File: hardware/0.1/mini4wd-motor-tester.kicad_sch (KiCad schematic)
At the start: 102 parts, among them J1 USB_C_Receptacle_USB2.0_16P, J2 JST SH, J3 JST SH, J4 JST XH, M1 Motor_DC, Q2 AO3401A, Q3 2N7002, SW1 RA, SW2 RA, SW3 EC11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

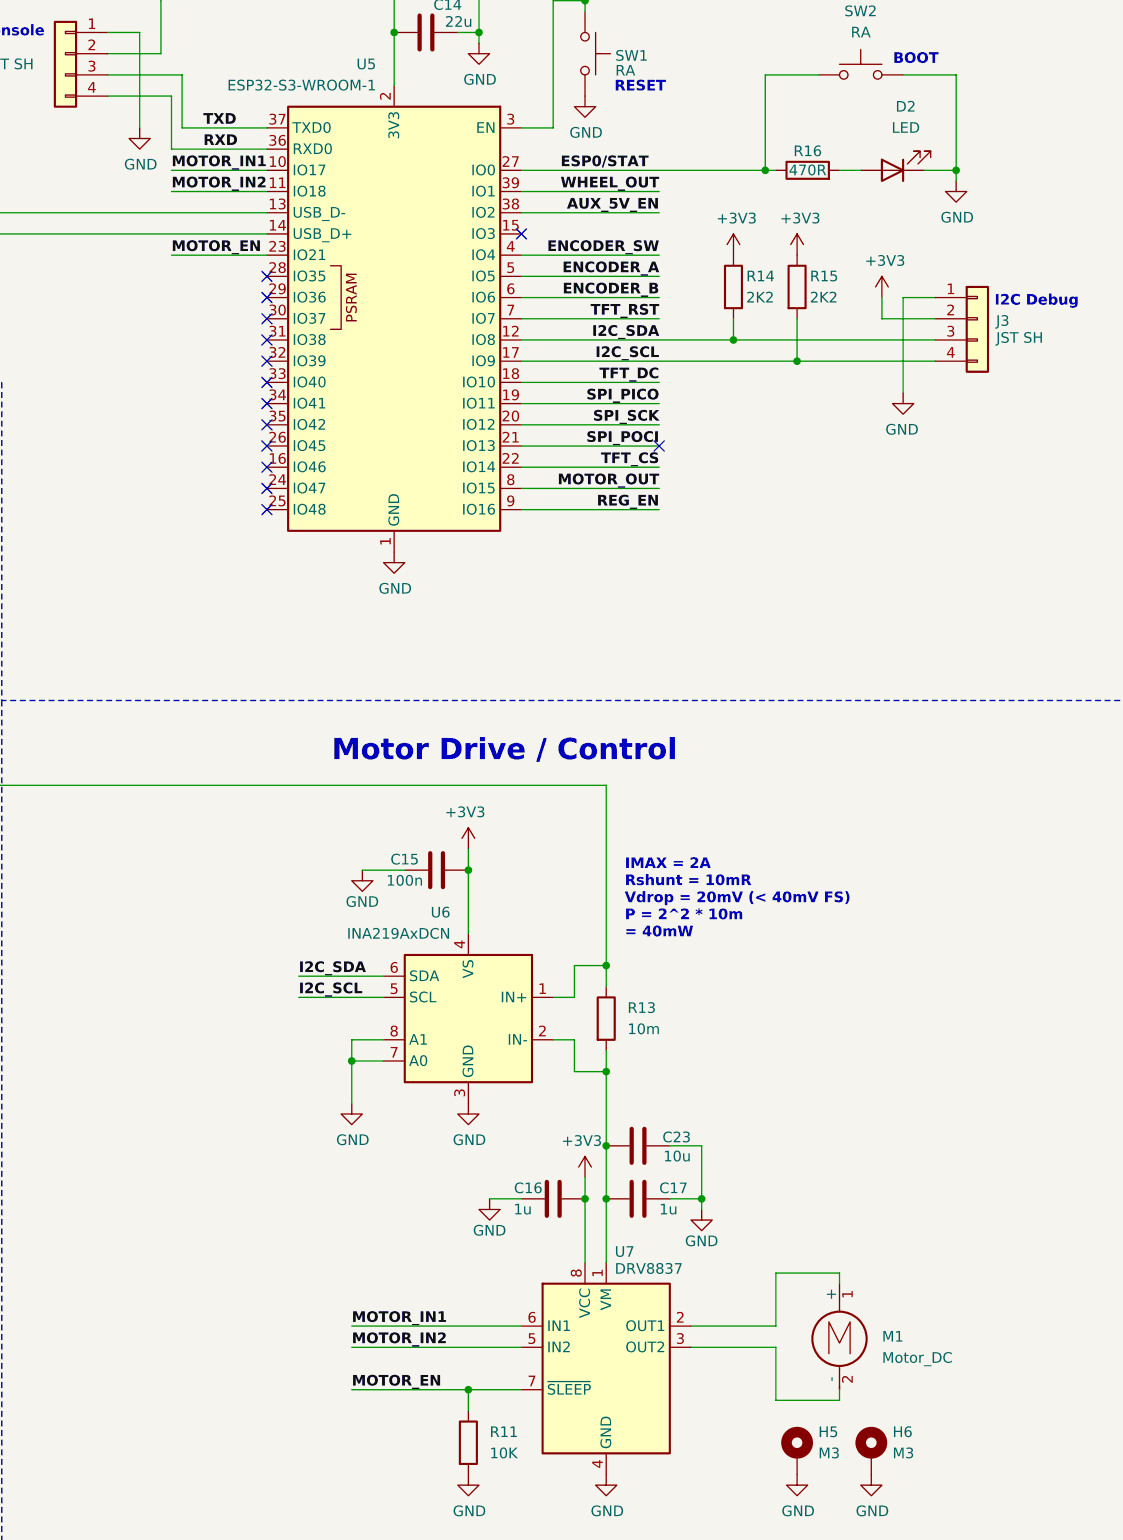
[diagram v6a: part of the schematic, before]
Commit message: board passing erc and drc
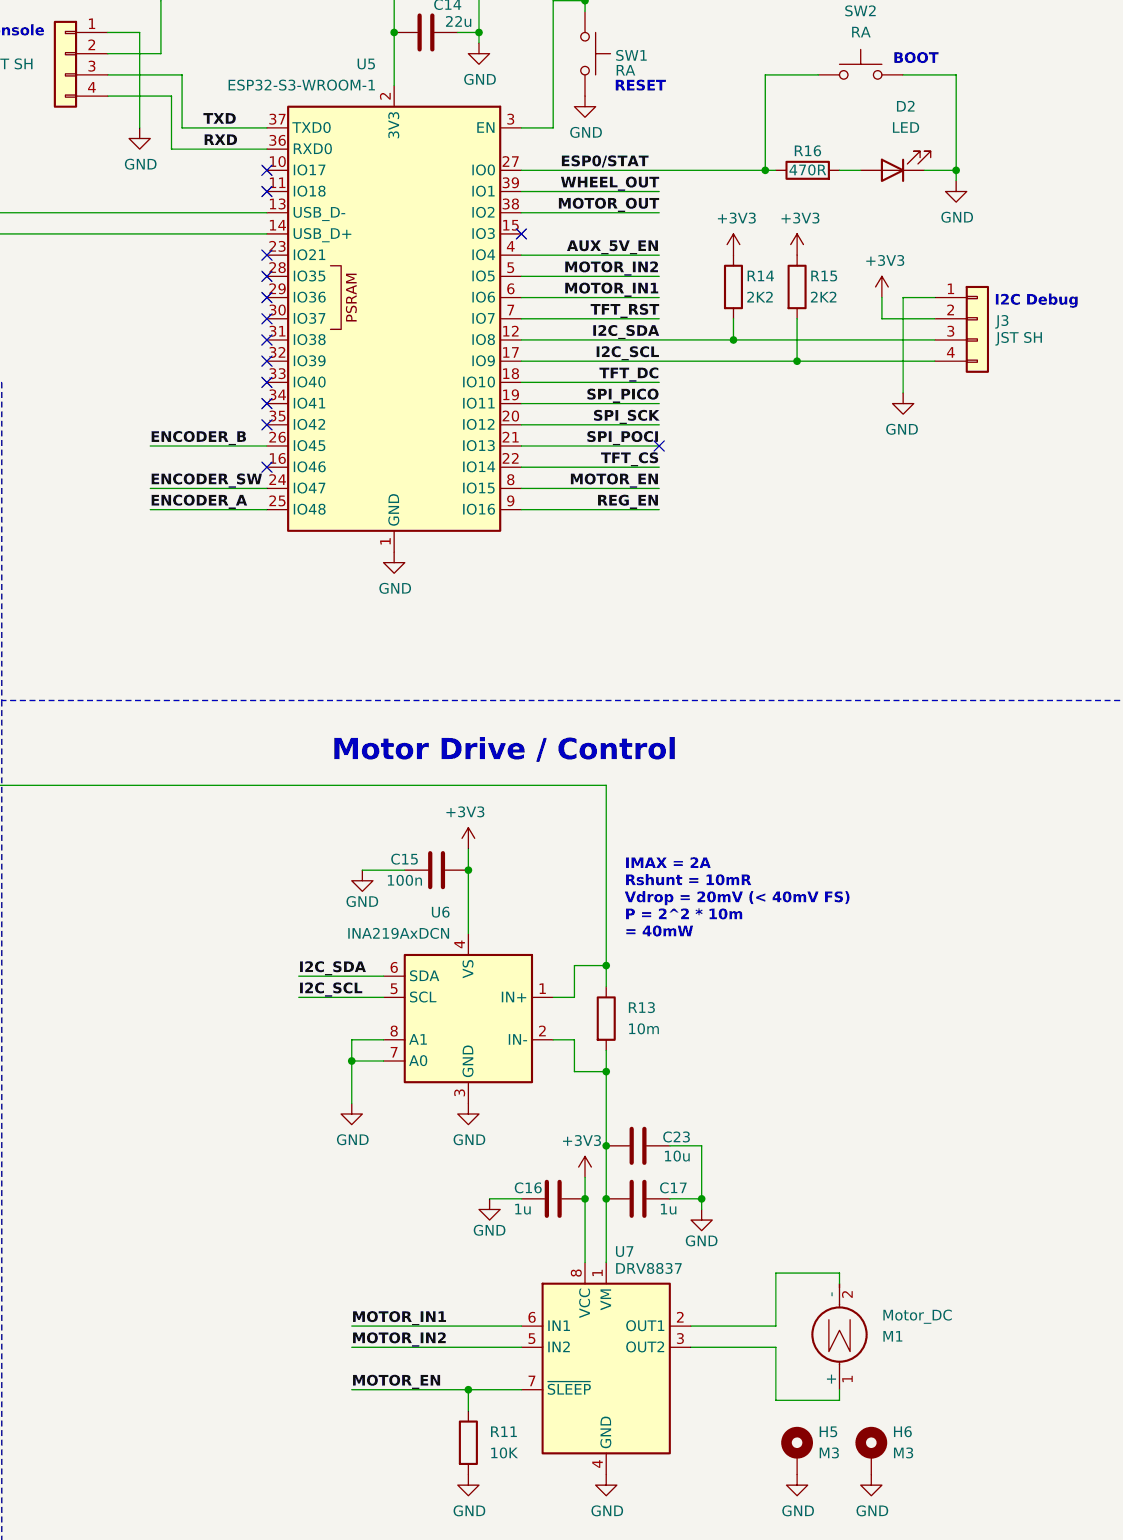
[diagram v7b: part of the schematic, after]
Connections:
- net AUX_5V_EN: now also U5.4 (IO4); no longer U5.38 (IO2)
- net ENCODER_A: now also U5.25 (IO48); no longer U5.5 (IO5)
- net ENCODER_B: now also U5.26 (IO45); no longer U5.6 (IO6)
- net ENCODER_SW: now also U5.24 (IO47); no longer U5.4 (IO4)
- net MOTOR_EN: now also U5.8 (IO15); no longer U5.23 (IO21)
- net MOTOR_IN1: now also U5.6 (IO6); no longer U5.10 (IO17)
- net MOTOR_IN2: now also U5.5 (IO5); no longer U5.11 (IO18)
- net MOTOR_OUT: now also U5.38 (IO2); no longer U5.8 (IO15)
- net at U7.2 (OUT1): now also M1.2 (-); no longer M1.1 (+)
- net at U7.3 (OUT2): now also M1.1 (+); no longer M1.2 (-)
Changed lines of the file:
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@@
 	)
 	(no_connect
-		(at 209.55 83.82)
-	)
-	(no_connect
 		(at 209.55 86.36)
 	)
 	(no_connect
-		(at 209.55 88.9)
+		(at 342.9 50.8)
 	)
 	(no_connect
-		(at 342.9 50.8)
+		(at 209.55 50.8)
 	)
 	(no_connect
@@
 	)
 	(no_connect
+		(at 209.55 60.96)
+	)
+	(no_connect
+		(at 209.55 53.34)
+	)
+	(no_connect
 		(at 209.55 63.5)
 	)
@@
 	)
 	(no_connect
-		(at 209.55 91.44)
-	)
-	(no_connect
 		(at 209.55 66.04)
 	)
@@
 	(wire
 		(pts
-			(xy 198.12 53.34) (xy 209.55 53.34)
-		)
-		(stroke
-			(width 0)
-			(type default)
-		)
-	)
-	(wire
-		(pts
 			(xy 339.09 46.99) (xy 339.09 48.26)
 		)
@@
 	(wire
 		(pts
+			(xy 195.58 83.82) (xy 209.55 83.82)
+		)
+		(stroke
+			(width 0)
+			(type default)
+		)
+	)
+	(wire
+		(pts
 			(xy 234.95 34.29) (xy 234.95 35.56)
 		)
@@
 	(wire
 		(pts
-			(xy 198.12 60.96) (xy 209.55 60.96)
-		)
-		(stroke
-			(width 0)
-			(type default)
-		)
-	)
-	(wire
-		(pts
 			(xy 153.67 106.68) (xy 153.67 107.95)
 		)
@@
 	(wire
 		(pts
-			(xy 246.38 149.86) (xy 246.38 146.05)
+			(xy 195.58 91.44) (xy 209.55 91.44)
 		)
 		(stroke
@@
 	(wire
 		(pts
-			(xy 198.12 50.8) (xy 209.55 50.8)
+			(xy 246.38 149.86) (xy 246.38 146.05)
 		)
 		(stroke
@@
 	(wire
 		(pts
+			(xy 195.58 88.9) (xy 209.55 88.9)
+		)
+		(stroke
+			(width 0)
+			(type default)
+		)
+	)
+	(wire
+		(pts
 			(xy 55.88 123.19) (xy 55.88 127)
 		)
@@
 	)
 	(label "ENCODER_SW"
-		(at 256.54 60.96 180)
+		(at 195.58 88.9 0)
 		(effects
 			(font
@@
 				(bold yes)
 			)
-			(justify right bottom)
+			(justify left bottom)
 		)
 	)
@@
 	)
 	(label "ENCODER_B"
-		(at 256.54 66.04 180)
+		(at 195.58 83.82 0)
 		(effects
 			(font
@@
 				(bold yes)
 			)
-			(justify right bottom)
+			(justify left bottom)
 		)
 	)
@@
 	)
 	(label "AUX_5V_EN"
-		(at 256.54 55.88 180)
+		(at 256.54 60.96 180)
 		(effects
 			(font
@@
 	)
 	(label "ENCODER_A"
-		(at 256.54 63.5 180)
+		(at 195.58 91.44 0)
 		(effects
 			(font
@@
 				(bold yes)
 			)
-			(justify right bottom)
+			(justify left bottom)
 		)
 	)
@@
 	)
 	(label "MOTOR_IN2"
-		(at 198.12 53.34 0)
+		(at 256.54 63.5 180)
 		(effects
 			(font
@@
 				(bold yes)
 			)
-			(justify left bottom)
+			(justify right bottom)
 		)
 	)
 	(label "MOTOR_OUT"
-		(at 256.54 88.9 180)
+		(at 256.54 55.88 180)
 		(effects
 			(font
@@
 	)
 	(label "MOTOR_EN"
-		(at 198.12 60.96 0)
+		(at 256.54 88.9 180)
 		(effects
 			(font
@@
 				(bold yes)
 			)
-			(justify left bottom)
+			(justify right bottom)
 		)
 	)
@@
 	)
 	(label "MOTOR_IN1"
-		(at 198.12 50.8 0)
+		(at 256.54 66.04 180)
 		(effects
 			(font
@@
 				(bold yes)
 			)
-			(justify left bottom)
+			(justify right bottom)
 		)
 	)
@@
 	(symbol
 		(lib_id "Motor:Motor_DC")
-		(at 278.13 189.23 0)
+		(at 278.13 191.77 0)
+		(mirror x)
 		(unit 1)
 		(exclude_from_sim no)
@@
 		(on_board yes)
 		(dnp no)
-		(fields_autoplaced yes)
 		(property "Reference" "M1"
-			(at 283.21 190.4999 0)
+			(at 283.21 190.5001 0)
 			(effects
 				(font
@@
 		)
 		(property "Value" "Motor_DC"
-			(at 283.21 193.0399 0)
+			(at 283.21 187.9601 0)
 			(effects
 				(font
@@
 		)
 		(property "Footprint" "josh-mechanical:Mini4WD_Motor"
-			(at 278.13 191.516 0)
+			(at 278.13 189.484 0)
 			(effects
 				(font
@@
 		)
 		(property "Datasheet" "~"
-			(at 278.13 191.516 0)
+			(at 278.13 189.484 0)
 			(effects
 				(font
@@
 		)
 		(property "Description" "DC Motor"
-			(at 278.13 189.23 0)
+			(at 278.13 191.77 0)
 			(effects
 				(font
@@
 		)
 		(property "JLCSMT" ""
-			(at 278.13 189.23 0)
+			(at 278.13 191.77 0)
 			(effects
 				(font

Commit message: off to fab
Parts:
- added F1: 2A, Fuse:Fuse_1206_3216Metric, symbol Device:Polyfuse
- added TP14: TP, TestPoint:TestPoint_Pad_D1.0mm, symbol Connector:TestPoint
- C12, C5, C6: value 1u -> 10u; footprint Capacitor_SMD:C_0603_1608Metric -> Capacitor_SMD:C_0805_2012Metric; LCSC C15849 -> C440198; MPN  CL10A105KB8NNNC -> GRM21BR61H106KE43L; Manufacturer Samsung Electro-Mechanics -> Murata
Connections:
- net +3V3: now also C12.1, TP14.1; no longer C12.2
- net +5V: now also C6.1; no longer C6.2
- net GND: now also C12.2, C5.2, C6.2; no longer C12.1, C5.1, C6.1
- net at J1.A4 (VBUS), J1.A9 (VBUS), J1.B4 (VBUS)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: now also F1.1; no longer C5.2, FB2.2
- new net: C5.1, F1.2, FB2.2
